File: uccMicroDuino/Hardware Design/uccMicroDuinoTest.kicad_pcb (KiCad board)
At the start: 2 copper layers, 30.4 x 28.6 mm, 14 parts, among them J1 USB_PCB_A, J2 Header, U1 ATtiny85-20SU

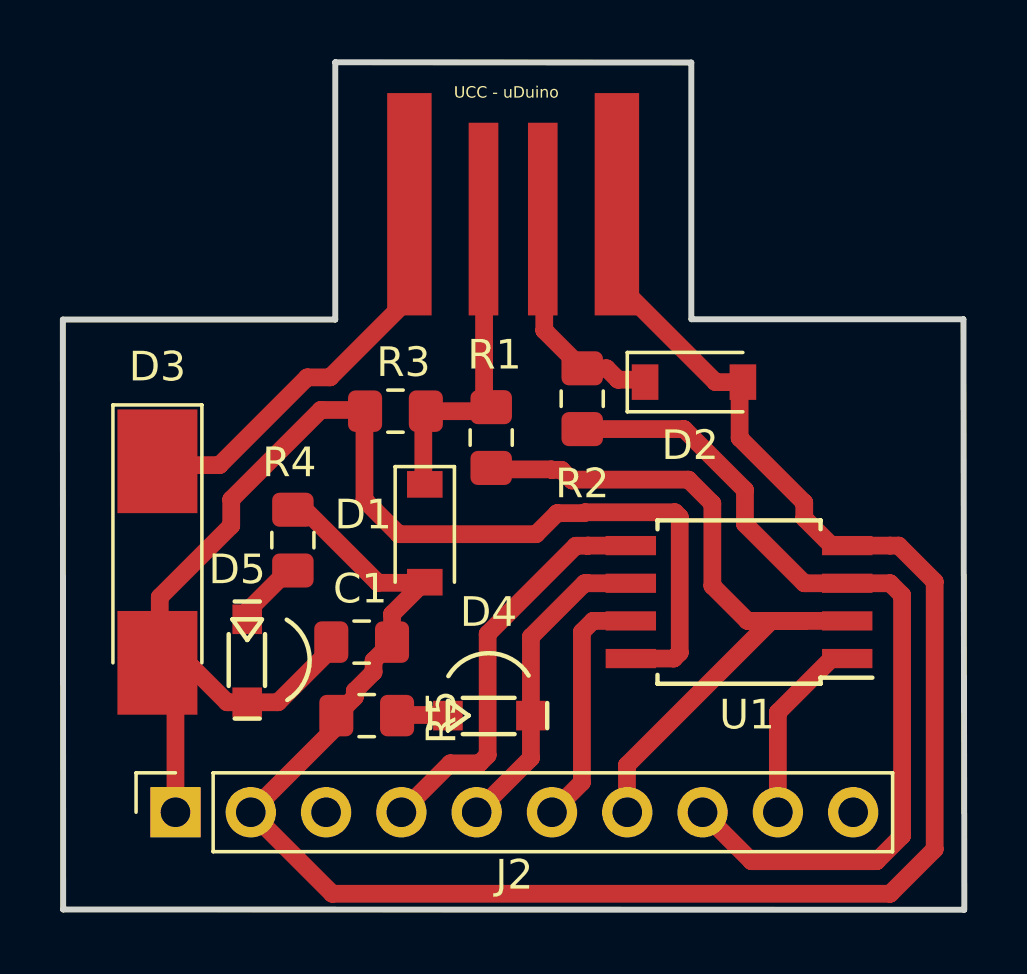
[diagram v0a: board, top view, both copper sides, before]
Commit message: Agregado modelo 3D y cerrado el poligono de placa
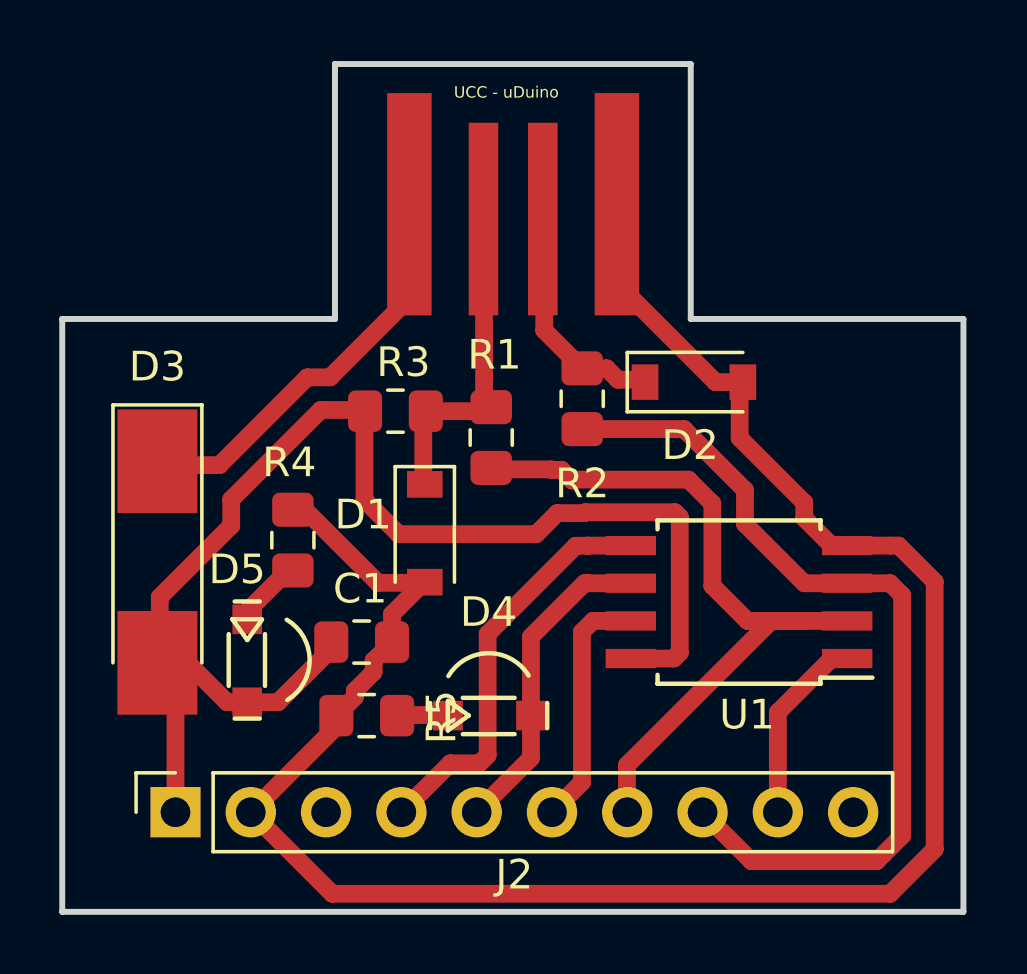
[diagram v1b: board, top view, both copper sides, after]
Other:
- outline, holes or cut-outs redrawn
